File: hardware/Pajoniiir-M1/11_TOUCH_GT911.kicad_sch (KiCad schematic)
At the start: 17 parts

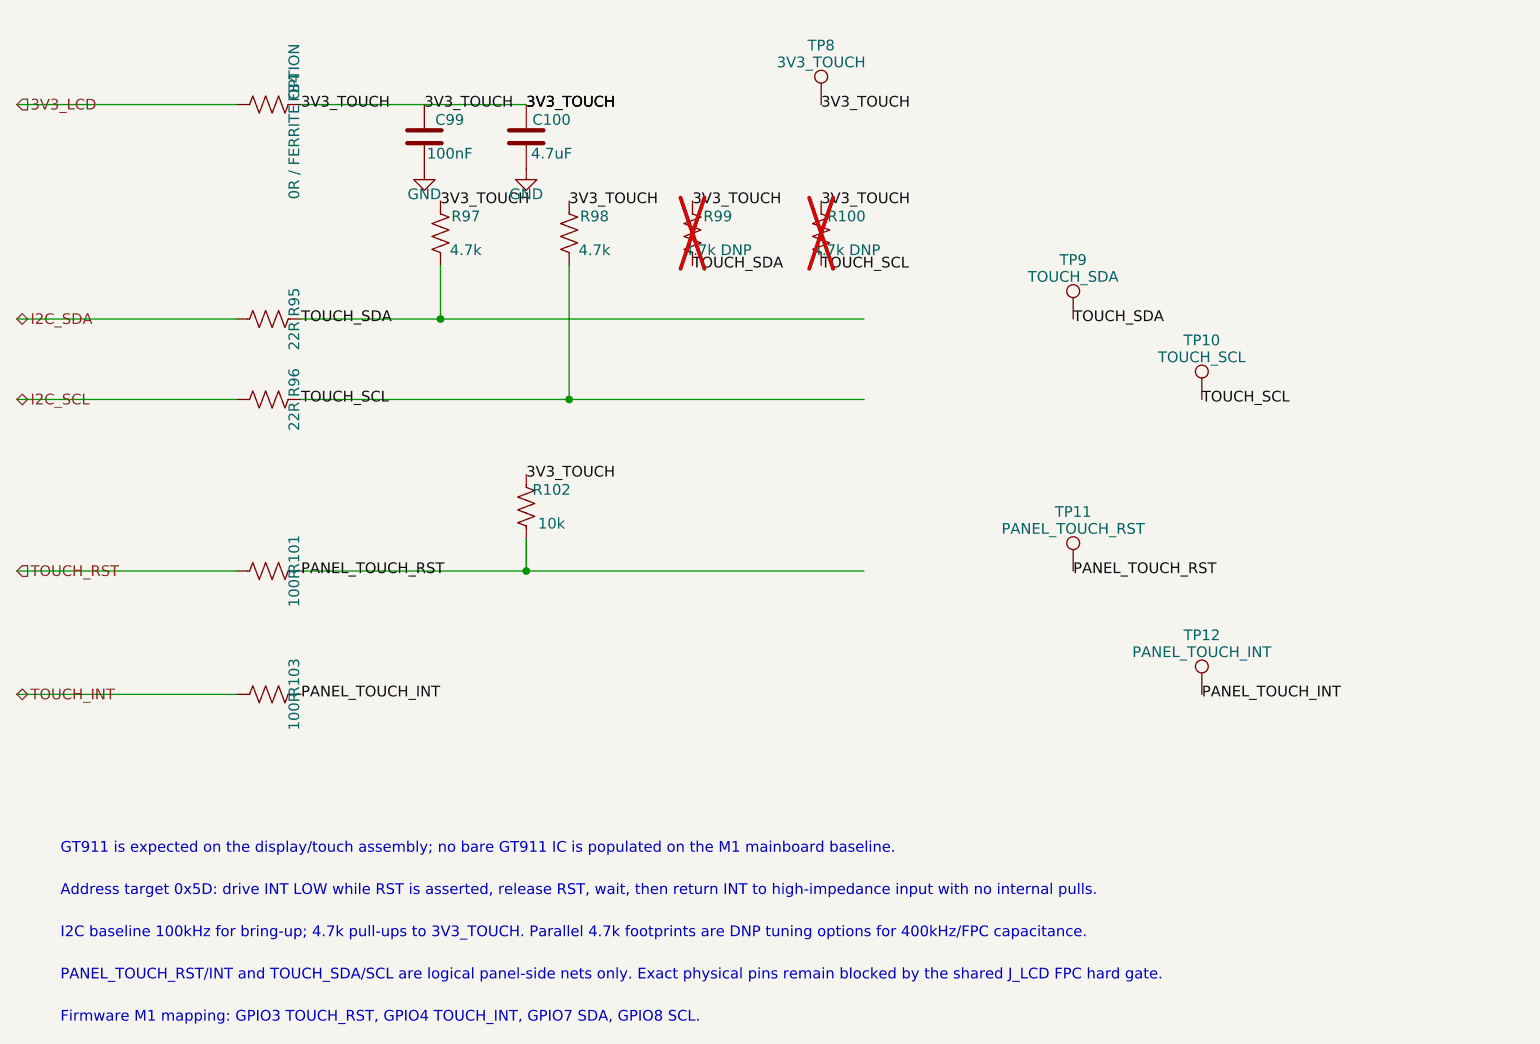
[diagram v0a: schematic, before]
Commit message: display: migrate schematic to final DSI506 module
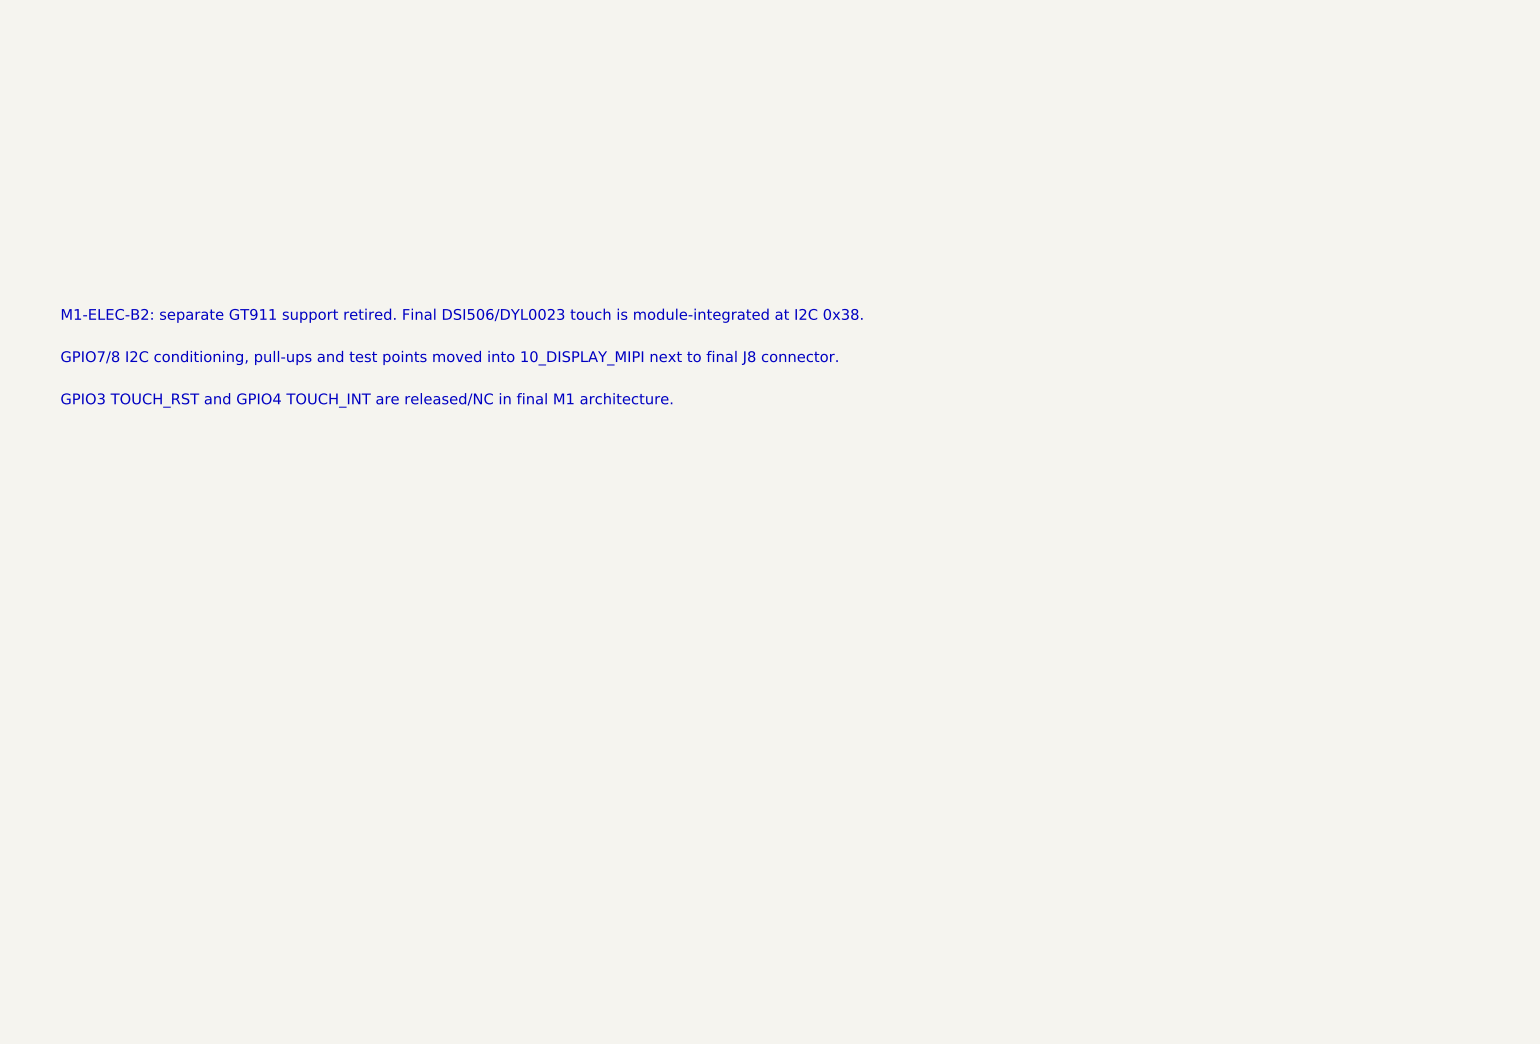
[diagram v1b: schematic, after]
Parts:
- removed C100: 4.7uF, Capacitor_SMD:C_0805_2012Metric, symbol Device:C
- removed C99: 100nF, Capacitor_SMD:C_0603_1608Metric, symbol Device:C
- removed FB4: 0R / FERRITE OPTION, Resistor_SMD:R_0603_1608Metric, symbol Device:R_US
- removed R100, R99: 4.7k DNP, Resistor_SMD:R_0603_1608Metric, symbol Device:R_US
- removed R101, R103: 100R, Resistor_SMD:R_0603_1608Metric, symbol Device:R_US
- removed R102: 10k, Resistor_SMD:R_0603_1608Metric, symbol Device:R_US
- removed R95, R96: 22R, Resistor_SMD:R_0402_1005Metric, symbol Device:R_US
- removed R97, R98: 4.7k, Resistor_SMD:R_0603_1608Metric, symbol Device:R_US
- removed TP10: TOUCH_SCL, TestPoint:TestPoint_Pad_D1.5mm, symbol Connector:TestPoint
- removed TP11: PANEL_TOUCH_RST, TestPoint:TestPoint_Pad_D1.5mm, symbol Connector:TestPoint
- removed TP12: PANEL_TOUCH_INT, TestPoint:TestPoint_Pad_D1.5mm, symbol Connector:TestPoint
- removed TP8: 3V3_TOUCH, TestPoint:TestPoint_Pad_D1.5mm, symbol Connector:TestPoint
- removed TP9: TOUCH_SDA, TestPoint:TestPoint_Pad_D1.5mm, symbol Connector:TestPoint
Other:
- note added: "GPIO3 TOUCH_RST and GPIO4 TOUCH_INT are released/NC in final M1 architecture."
- note added: "GPIO7/8 I2C conditioning, pull-ups and test points moved into 10_DISPLAY_MIPI next to final J8 connector."
- note added: "M1-ELEC-B2: separate GT911 support retired. Final DSI506/DYL0023 touch is module-integrated at I2C 0x38."
- note removed: "Address target 0x5D: drive INT LOW while RST is asserted, release RST, wait, then return INT to high-impedance input with no internal pulls."
- note removed: "Firmware M1 mapping: GPIO3 TOUCH_RST, GPIO4 TOUCH_INT, GPIO7 SDA, GPIO8 SCL."
- note removed: "GT911 is expected on the display/touch assembly; no bare GT911 IC is populated on the M1 mainboard baseline."
- note removed: "I2C baseline 100kHz for bring-up; 4.7k pull-ups to 3V3_TOUCH. Parallel 4.7k footprints are DNP tuning options for 400kHz/FPC capacitance."
- note removed: "PANEL_TOUCH_RST/INT and TOUCH_SDA/SCL are logical panel-side nets only. Exact physical pins remain blocked by the shared J_LCD FPC hard gate."
- title: Pajoniiir-M1 Rev A — 11_TOUCH_GT911 -> Pajoniiir-M1 Rev A — 11_TOUCH_GT911 RETIRED

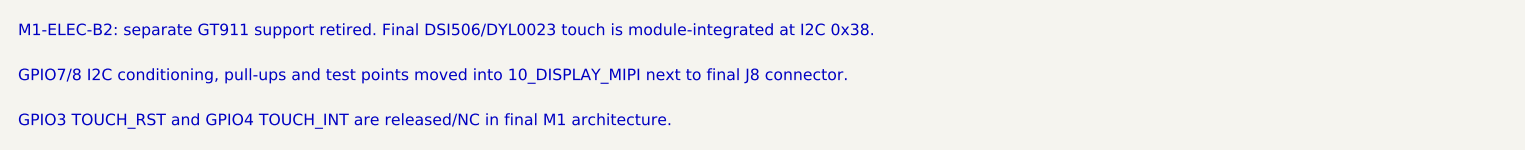
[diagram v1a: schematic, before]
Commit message: feat: establish board-first B8 pre-layout
Populate the live PCB with the complete schematic footprint/net set, preserve fail-closed mechanical gates, and isolate DSI506 as a qualified display profile. Add reproducible placement validation, ERC/BOM evidence, and synchronized project documentation.
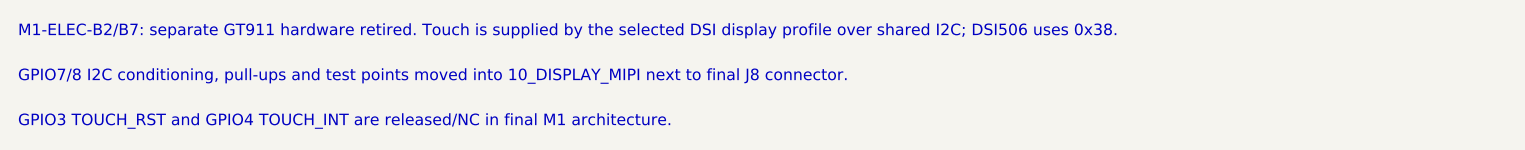
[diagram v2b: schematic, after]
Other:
- note added: "M1-ELEC-B2/B7: separate GT911 hardware retired. Touch is supplied by the selected DSI display profile over shared I2C; DSI506 uses 0x38."
- note removed: "M1-ELEC-B2: separate GT911 support retired. Final DSI506/DYL0023 touch is module-integrated at I2C 0x38."
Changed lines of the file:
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@@
     (rev "B / M1-ELEC-B2")
     (company "Pajoniiir")
-    (comment 1 "Retired: final DSI506 touch is integrated through J8 shared I2C")
+    (comment 1 "Retired: supported DSI modules provide touch through J6 shared I2C")
     (comment 2 "No GT911 RST/INT/address-select network on final M1")
   )
-  (text "M1-ELEC-B2: separate GT911 support retired. Final DSI506/DYL0023 touch is module-integrated at I2C 0x38." (exclude_from_sim no) (at 35 55 0) (effects (font (size 1.27 1.27)) (justify left)))
+  (text "M1-ELEC-B2/B7: separate GT911 hardware retired. Touch is supplied by the selected DSI display profile over shared I2C; DSI506 uses 0x38." (exclude_from_sim no) (at 35 55 0) (effects (font (size 1.27 1.27)) (justify left)))
   (text "GPIO7/8 I2C conditioning, pull-ups and test points moved into 10_DISPLAY_MIPI next to final J8 connector." (exclude_from_sim no) (at 35 60 0) (effects (font (size 1.27 1.27)) (justify left)))
   (text "GPIO3 TOUCH_RST and GPIO4 TOUCH_INT are released/NC in final M1 architecture." (exclude_from_sim no) (at 35 65 0) (effects (font (size 1.27 1.27)) (justify left)))
